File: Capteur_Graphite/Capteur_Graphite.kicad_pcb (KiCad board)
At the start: 2 copper layers, 68.6 x 53.3 mm, 25 parts, among them J1 Power, J2 Digital/PWM, J3 Analog, J4 Digital/PWM, U1 LTC1050ACN8_PBF, U2 MCP41050

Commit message: Version Finale 4 le retour
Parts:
- moved Bluetooth1 6.75 mm to (145.5, 61.5)
- moved U2 2.12 mm to (119.5, 66.5)
- moved Servor1 2.06 mm to (133.5, 60.0)
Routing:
- net +5: track 132.8 -> 241.0 mm
- net TX: track 7.54 -> 15.8 mm
- net RX: track 6.54 -> 13.8 mm
- net 13: track 44.4 -> 37.6 mm
- net 11: track 17.8 -> 15.9 mm
- net ServoOut: track 8.79 -> 10.6 mm
- net 10: track 15.8 -> 14.0 mm
- net P2: track 16.2 -> 15.1 mm
- net P4: track 11.7 -> 10.8 mm
- net A0: track 10.00 -> 9.29 mm
- net Net-(U1-OUT): track 26.1 -> 25.6 mm

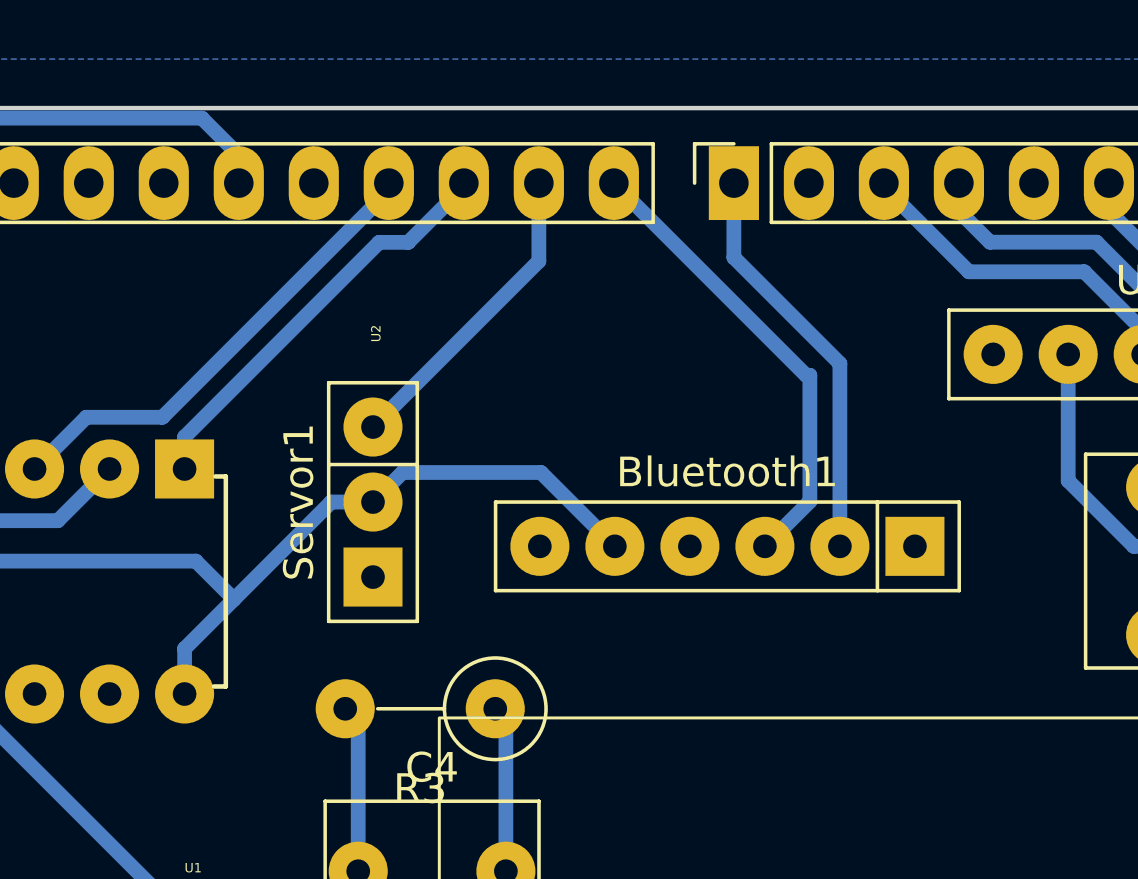
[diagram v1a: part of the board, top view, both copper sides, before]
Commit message: repositionement 3D
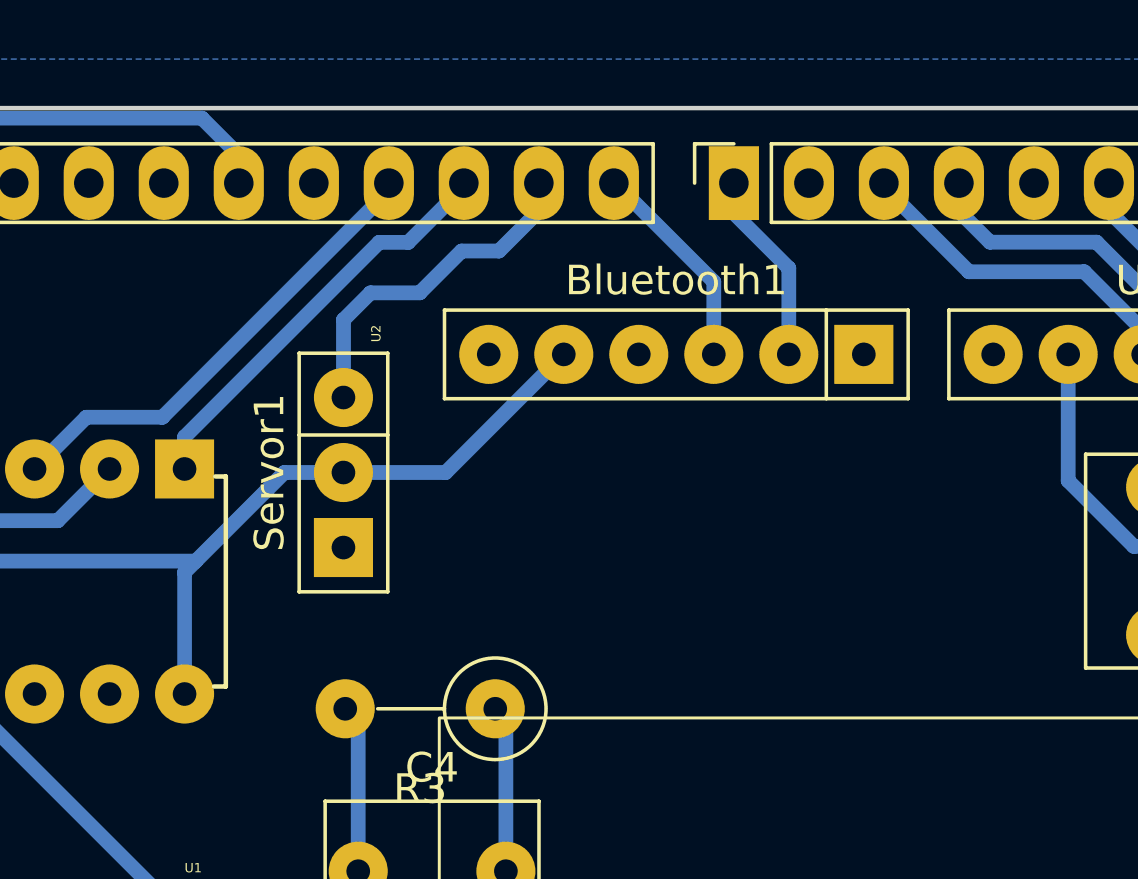
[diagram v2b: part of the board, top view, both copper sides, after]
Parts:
- moved Bluetooth1 6.73 mm to (143.8, 55.0)
- moved Servor1 1.41 mm to (132.5, 59.0)
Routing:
- net TX: track 15.8 -> 7.23 mm
- net RX: track 13.8 -> 6.57 mm
- net +5: track 241.0 -> 239.5 mm
- net ServoOut: track 10.6 -> 11.7 mm
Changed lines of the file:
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@@
 	(footprint "Librairie empreinte:Bluetooth"
 		(layer "F.Cu")
-		(at 145.5 61.5 180)
+		(at 143.77 55 180)
 		(property "Reference" "Bluetooth1"
 			(at 0 2.5 180)
@@
 	(footprint "Librairie empreinte:ServoMotor"
 		(layer "F.Cu")
-		(at 133.5 60 -90)
+		(at 132.5 59 -90)
 		(property "Reference" "Servor1"
 			(at 0 2.5 90)
@@
 	)
 	(segment
+		(start 132.5 59)
+		(end 130.5 59)
+		(width 0.5)
+		(layer "B.Cu")
+		(net 21)
+	)
+	(segment
 		(start 127.5 62)
 		(end 118.728084 62)
@@
 	)
 	(segment
-		(start 101.5 75.085787)
-		(end 102.085787 74.5)
+		(start 139.96 55)
+		(end 135.96 59)
 		(width 0.5)
 		(layer "B.Cu")
@@
 	)
 	(segment
-		(start 141.69 61.5)
-		(end 139.19 59)
+		(start 101.5 75.085787)
+		(end 102.085787 74.5)
 		(width 0.5)
 		(layer "B.Cu")
@@
 	)
 	(segment
-		(start 139.151 99.461)
-		(end 138.1 98.41)
+		(start 127.12 62.38)
+		(end 127.5 62)
 		(width 0.5)
 		(layer "B.Cu")
@@
 	)
 	(segment
-		(start 139.19 59)
-		(end 134.5 59)
+		(start 139.151 99.461)
+		(end 138.1 98.41)
 		(width 0.5)
 		(layer "B.Cu")
@@
 	)
 	(segment
-		(start 132.085787 60)
-		(end 128.792894 63.292894)
-		(width 0.5)
-		(layer "B.Cu")
-		(net 21)
-	)
-	(segment
 		(start 167.718966 61.5)
 		(end 168.254 62.035034)
@@
 	)
 	(segment
-		(start 133.5 60)
-		(end 132.085787 60)
-		(width 0.5)
-		(layer "B.Cu")
-		(net 21)
-	)
-	(segment
 		(start 100.326 48.674)
 		(end 100.326 71.326)
@@
 	)
 	(segment
-		(start 148 84)
-		(end 153.5 84)
+		(start 135.96 59)
+		(end 132.5 59)
 		(width 0.5)
 		(layer "B.Cu")
@@
 	)
 	(segment
-		(start 138.1 98.41)
-		(end 137.01 99.5)
+		(start 148 84)
+		(end 153.5 84)
 		(width 0.5)
 		(layer "B.Cu")
@@
 	)
 	(segment
-		(start 134.5 59)
-		(end 133.5 60)
+		(start 138.1 98.41)
+		(end 137.01 99.5)
 		(width 0.5)
 		(layer "B.Cu")
@@
 	)
 	(segment
-		(start 128.792894 63.292894)
-		(end 127.12 64.965787)
-		(width 0.5)
-		(layer "B.Cu")
-		(net 21)
-	)
-	(segment
 		(start 102.085787 74.5)
 		(end 103.5 74.5)
@@
 	)
 	(segment
-		(start 128.792894 63.292894)
-		(end 127.5 62)
-		(width 0.5)
-		(layer "B.Cu")
-		(net 21)
-	)
-	(segment
 		(start 148 97.844156)
 		(end 148 84)
@@
 	)
 	(segment
+		(start 127.12 66.5)
+		(end 127.12 62.38)
+		(width 0.5)
+		(layer "B.Cu")
+		(net 21)
+	)
+	(segment
 		(start 168.254 62.035034)
 		(end 168.254 77.246)
@@
 	)
 	(segment
-		(start 127.12 64.965787)
-		(end 127.12 66.5)
+		(start 130.5 59)
+		(end 127.5 62)
 		(width 0.5)
 		(layer "B.Cu")
@@
 	)
 	(segment
-		(start 149.31 55.31)
-		(end 149.31 61.5)
+		(start 147.58 55)
+		(end 147.58 52.08)
 		(width 0.5)
 		(layer "B.Cu")
@@
 	)
 	(segment
-		(start 145.72 51.72)
-		(end 149.31 55.31)
+		(start 147.58 52.08)
+		(end 145.72 50.22)
 		(width 0.5)
 		(layer "B.Cu")
@@
 	)
 	(segment
-		(start 145.72 49.2)
-		(end 145.72 51.72)
+		(start 145.72 50.22)
+		(end 145.72 49.2)
 		(width 0.5)
 		(layer "B.Cu")
@@
 	)
 	(segment
-		(start 148.163814 55.707814)
+		(start 141.7 49.2)
 		(end 141.656 49.2)
 		(width 0.5)
@@
 	)
 	(segment
-		(start 148.292186 59.977814)
-		(end 148.292186 55.707814)
-		(width 0.5)
-		(layer "B.Cu")
-		(net 29)
-	)
-	(segment
-		(start 148.292186 55.707814)
-		(end 148.163814 55.707814)
+		(start 145.04 55)
+		(end 145.04 52.54)
 		(width 0.5)
 		(layer "B.Cu")
@@
 	)
 	(segment
-		(start 146.77 61.5)
-		(end 148.292186 59.977814)
+		(start 145.04 52.54)
+		(end 141.7 49.2)
 		(width 0.5)
 		(layer "B.Cu")
@@
 	)
 	(segment
-		(start 133.5 57.46)
-		(end 139.116 51.844)
+		(start 139.116 50.15)
+		(end 139.116 49.2)
 		(width 0.5)
 		(layer "B.Cu")
@@
 	)
 	(segment
-		(start 139.116 51.844)
-		(end 139.116 49.2)
+		(start 132.5 53.831256)
+		(end 133.415628 52.915628)
+		(width 0.5)
+		(layer "B.Cu")
+		(net 31)
+	)
+	(segment
+		(start 135.084372 52.915628)
+		(end 136.5 51.5)
+		(width 0.5)
+		(layer "B.Cu")
+		(net 31)
+	)
+	(segment
+		(start 136.5 51.5)
+		(end 137.766 51.5)
+		(width 0.5)
+		(layer "B.Cu")
+		(net 31)
+	)
+	(segment
+		(start 132.5 56.46)
+		(end 132.5 53.831256)
+		(width 0.5)
+		(layer "B.Cu")
+		(net 31)
+	)
+	(segment
+		(start 133.415628 52.915628)
+		(end 135.084372 52.915628)
+		(width 0.5)
+		(layer "B.Cu")
+		(net 31)
+	)
+	(segment
+		(start 137.766 51.5)
+		(end 139.116 50.15)
 		(width 0.5)
 		(layer "B.Cu")
